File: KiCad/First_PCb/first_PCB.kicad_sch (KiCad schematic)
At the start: 0 parts

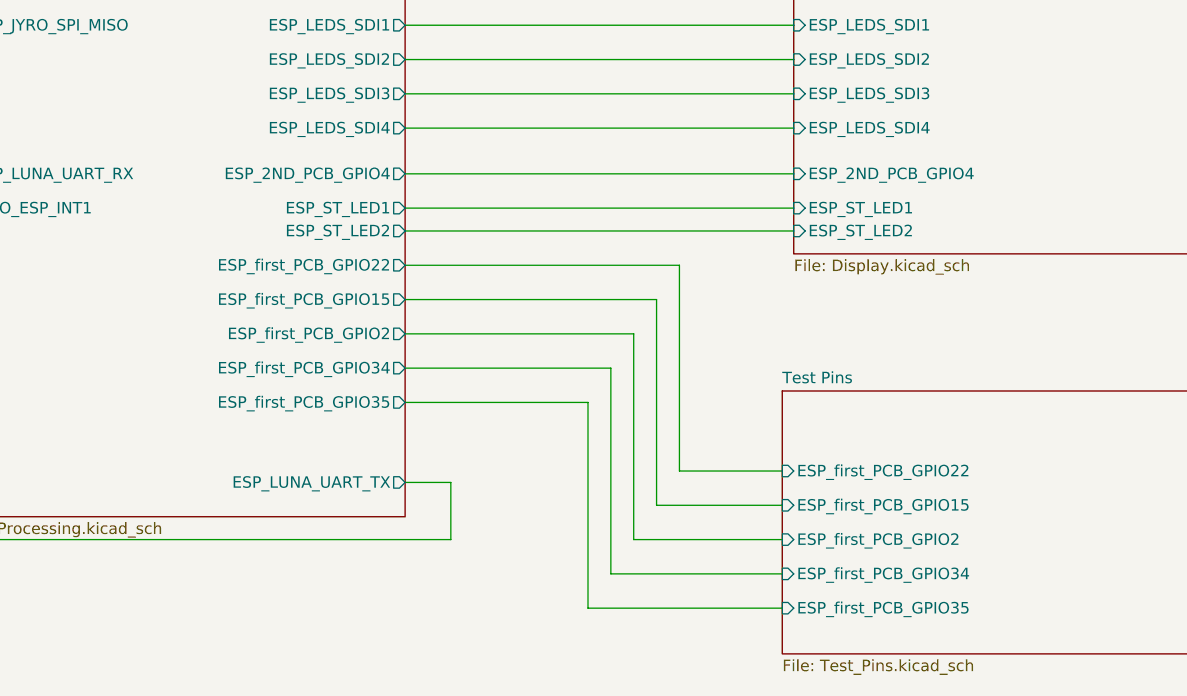
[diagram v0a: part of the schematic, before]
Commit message: added all the kicad files & gerbers of the first pcb
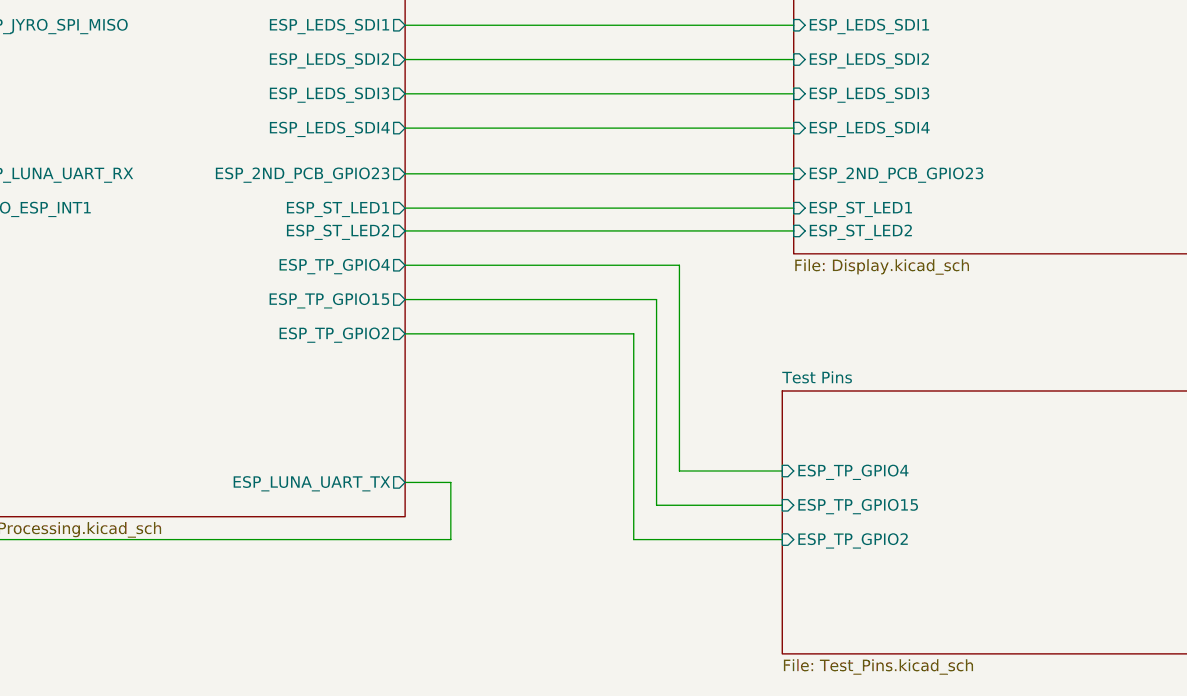
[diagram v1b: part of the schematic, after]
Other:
- sheet Display ports: added ESP_2ND_PCB_GPIO23; removed ESP_2ND_PCB_GPIO4
- sheet Processing ports: added ESP_2ND_PCB_GPIO23, ESP_TP_GPIO15, ESP_TP_GPIO2, ESP_TP_GPIO4; removed ESP_2ND_PCB_GPIO4, ESP_first_PCB_GPIO15, ESP_first_PCB_GPIO2, ESP_first_PCB_GPIO22, ESP_first_PCB_GPIO34, ESP_first_PCB_GPIO35
- sheet Test Pins ports: added ESP_TP_GPIO15, ESP_TP_GPIO2, ESP_TP_GPIO4; removed ESP_first_PCB_GPIO15, ESP_first_PCB_GPIO2, ESP_first_PCB_GPIO22, ESP_first_PCB_GPIO34, ESP_first_PCB_GPIO35
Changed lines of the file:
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@@
-	(wire
-		(pts
-			(xy 214.63 140.97) (xy 195.58 140.97)
-		)
-		(stroke
-			(width 0)
-			(type default)
-		)
-	)
 	(wire
 		(pts
@@
 	(wire
 		(pts
-			(xy 193.04 144.78) (xy 193.04 121.92)
-		)
-		(stroke
-			(width 0)
-			(type default)
-		)
-	)
-	(wire
-		(pts
 			(xy 172.72 106.68) (xy 203.2 106.68)
 		)
@@
 	(wire
 		(pts
-			(xy 214.63 144.78) (xy 193.04 144.78)
-		)
-		(stroke
-			(width 0)
-			(type default)
-		)
-	)
-	(wire
-		(pts
 			(xy 177.8 137.16) (xy 177.8 130.81)
 		)
@@
 	(wire
 		(pts
-			(xy 172.72 121.92) (xy 193.04 121.92)
-		)
-		(stroke
-			(width 0)
-			(type default)
-		)
-	)
-	(wire
-		(pts
 			(xy 172.72 96.52) (xy 215.9 96.52)
 		)
@@
 	(wire
 		(pts
-			(xy 195.58 140.97) (xy 195.58 118.11)
-		)
-		(stroke
-			(width 0)
-			(type default)
-		)
-	)
-	(wire
-		(pts
 			(xy 24.13 85.09) (xy 33.02 85.09)
 		)
@@
 		(pts
 			(xy 200.66 133.35) (xy 200.66 110.49)
-		)
-		(stroke
-			(width 0)
-			(type default)
-		)
-	)
-	(wire
-		(pts
-			(xy 172.72 118.11) (xy 195.58 118.11)
 		)
 		(stroke
@@
 			)
 		)
-		(pin "ESP_2ND_PCB_GPIO4" input
+		(pin "ESP_2ND_PCB_GPIO23" input
 			(at 215.9 96.52 180)
 			(effects
@@
 			)
 		)
-		(pin "ESP_first_PCB_GPIO2" input
+		(pin "ESP_TP_GPIO2" input
 			(at 214.63 137.16 180)
 			(effects
@@
 			)
 		)
-		(pin "ESP_first_PCB_GPIO15" input
+		(pin "ESP_TP_GPIO15" input
 			(at 214.63 133.35 180)
 			(effects
@@
 			)
 		)
-		(pin "ESP_first_PCB_GPIO22" input
+		(pin "ESP_TP_GPIO4" input
 			(at 214.63 129.54 180)
-			(effects
-				(font
-					(size 1.27 1.27)
-				)
-				(justify left)
-			)
-		)
-		(pin "ESP_first_PCB_GPIO34" input
-			(at 214.63 140.97 180)
-			(effects
-				(font
-					(size 1.27 1.27)
-				)
-				(justify left)
-			)
-		)
-		(pin "ESP_first_PCB_GPIO35" input
-			(at 214.63 144.78 180)
 			(effects
 				(font
@@
 			)
 		)
-		(pin "ESP_2ND_PCB_GPIO4" output
+		(pin "ESP_2ND_PCB_GPIO23" output
 			(at 172.72 96.52 0)
 			(effects
@@
 			)
 		)
-		(pin "ESP_first_PCB_GPIO22" output
+		(pin "ESP_TP_GPIO4" output
 			(at 172.72 106.68 0)
 			(effects
@@
 			)
 		)
-		(pin "ESP_first_PCB_GPIO2" output
+		(pin "ESP_TP_GPIO2" output
 			(at 172.72 114.3 0)
 			(effects
@@
 			)
 		)
-		(pin "ESP_first_PCB_GPIO15" output
+		(pin "ESP_TP_GPIO15" output
 			(at 172.72 110.49 0)
 			(effects
 				(font
-					(size 1.27 1.27)
-				)
-				(justify right)
-			)
-		)
-		(pin "ESP_first_PCB_GPIO34" output
-			(at 172.72 118.11 0)
-			(effects
-				(font
-					(size 1.27 1.27)
-				)
-				(justify right)
-			)
-		)
-		(pin "ESP_first_PCB_GPIO35" output
-			(at 172.72 121.92 0)
-			(effects
-				(font
